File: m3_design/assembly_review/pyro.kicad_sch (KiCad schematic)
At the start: 32 parts, among them J120 ARM: RAW / BUS2 / BUS1 / RAW, J121 E1- / E1+ / E2+ / E2-, Q124 AON7524, Q125 AON7524

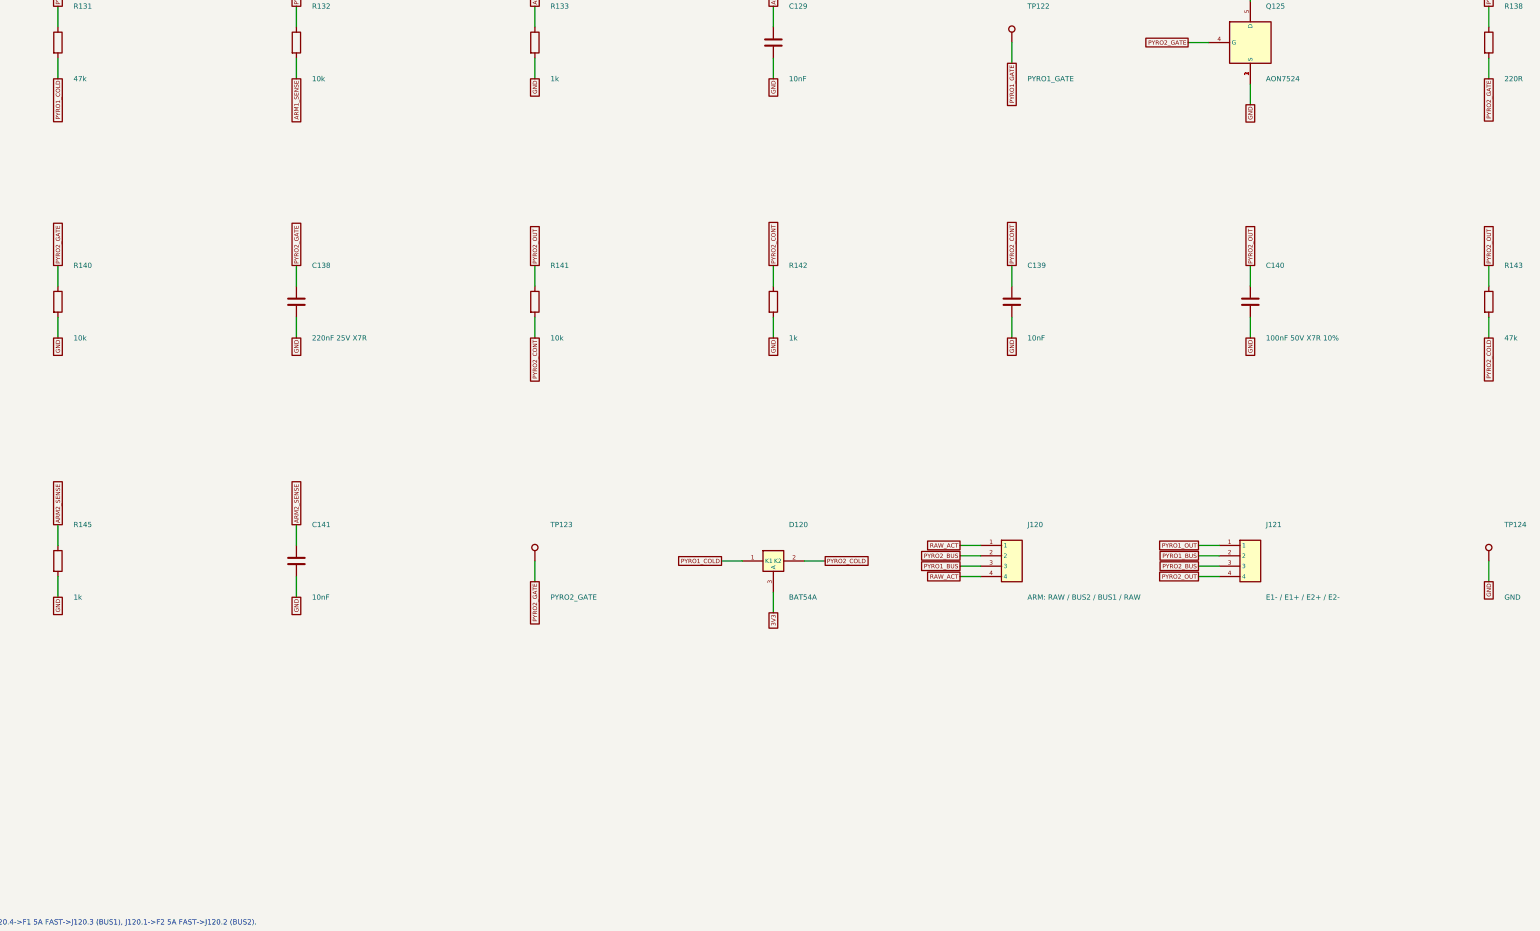
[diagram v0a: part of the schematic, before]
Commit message: Limit a shorted igniter to ~4 A: R134/R135 2 ohm pulse resistors, 10k cold pull-ups
Simulation of R2 as merged showed that firing into a shorted igniter pulled
BAT_IN below 5 V for 4-20 ms until the 5 A arming fuse melted (MCU reset,
channel 2 lost) and overstressed the AON7524 at a fresh pack.

- R134/R135 Bourns CRM2512-FX-2R00ELF (C3013496) in series between each fused
  bus and the igniter terminal (new nets PYRO1_IGN/PYRO2_IGN); arm sense stays
  on the plug side. Placed in line on the bus straps; TP124 moved, four
  references moved to free silkscreen.
- R131/R143 cold pull-ups 47k -> 10k for plug-out self-test margin.
- check_actuators.py contract updated (+ negative cases verified by hand).
- sim_r2 models the fix as drawn: all current-design cases pass; the merged
  design is kept as OLD-FAIL comparison rows.
- Firmware requirements recorded: 20 ms fire pulse, resume after reset.

DRC 0 / unconnected 0 / parity 0 / ERC 0, audit OK; diagnostics 173, firmware
112, quality_audit 12 tests pass.

Co-Authored-By: Claude Opus 5.5 (1M context) <noreply@anthropic.com>
Claude-Session: https://claude.ai/code/session_01DdkfTxR7SVyv9xZNmPk9vB
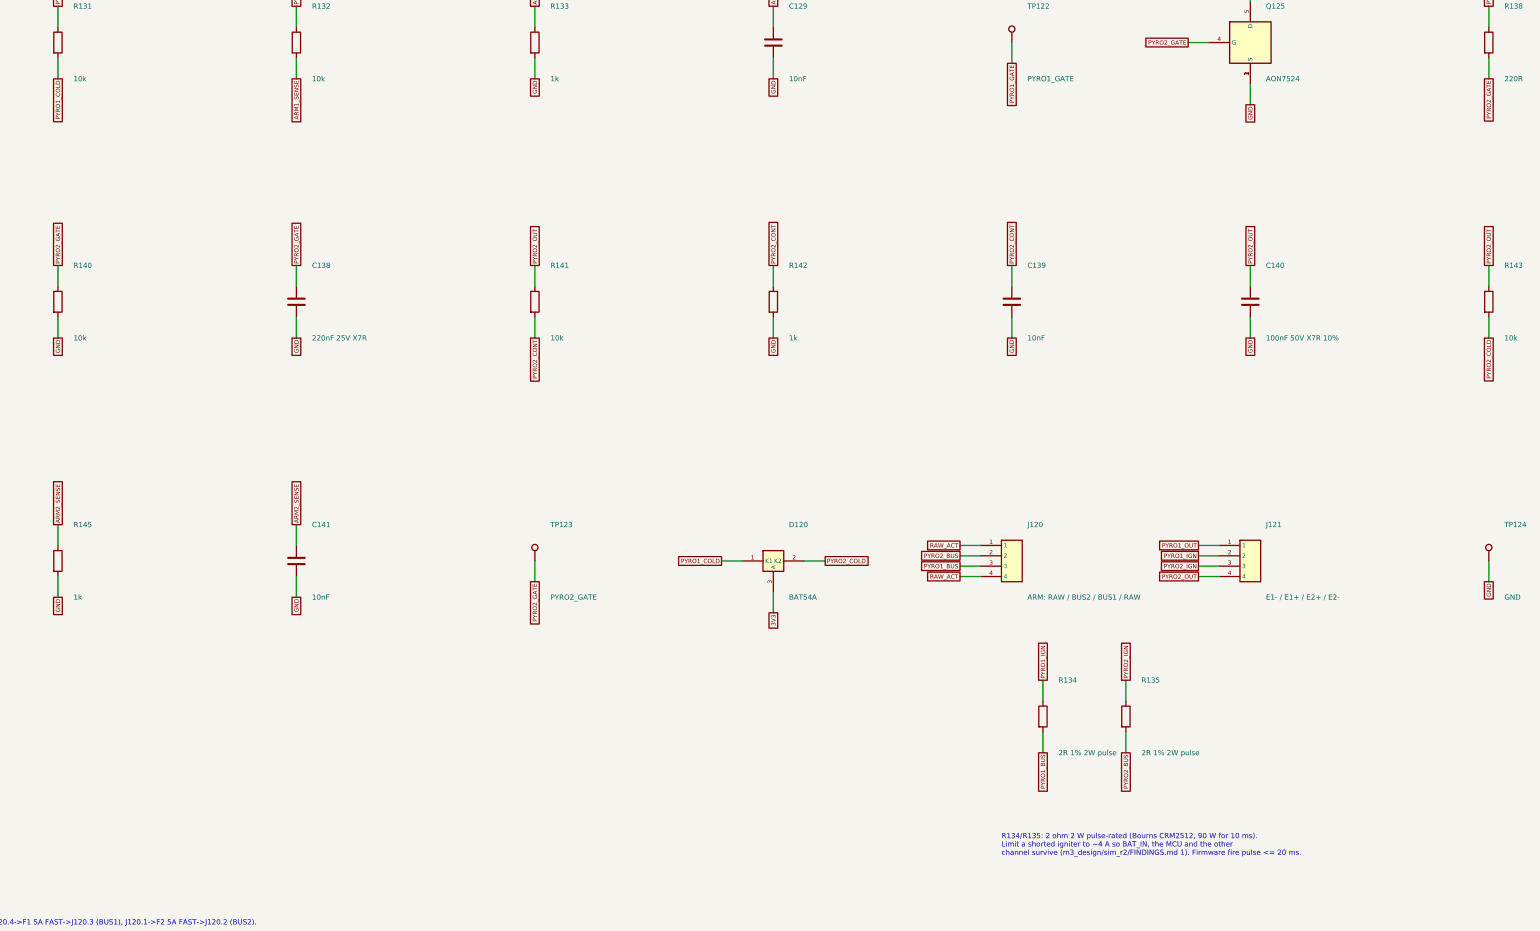
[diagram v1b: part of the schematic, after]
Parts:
- added R134, R135: 2R 1% 2W pulse, rocket:R2512, symbol M3:R
- R131, R143: value 47k -> 10k; LCSC C25792 -> C25744
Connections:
- net PYRO1_BUS: now also R134.2; no longer J121.2
- net PYRO2_BUS: now also R135.2; no longer J121.3
- new net PYRO1_IGN: J121.2, R134.1
- new net PYRO2_IGN: J121.3, R135.1
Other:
- note added: "R134/R135: 2 ohm 2 W pulse-rated (Bourns CRM2512, 90 W for 10 ms). Limit a shorted igniter to ~4 A so BAT_IN, the MCU and the other channel survive (m3_design/sim_r2/FINDINGS.md 1). Firmware fire pulse <= 20 ms."
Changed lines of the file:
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@@
 					(size 1.27 1.27))
 				(justify left)))
-		(property "Value" "47k"
+		(property "Value" "10k"
 			(at 102.87 123.19 0)
 			(effects
@@
 				(font
 					(size 1.27 1.27))))
-		(property "LCSC" "C25792"
+		(property "LCSC" "C25744"
 			(at 99.06 114.3 0)
 			(hide yes)
@@
 					(reference "R132")
 					(unit 1)))))
+	(symbol
+		(lib_id "M3:R")
+		(at 340.36 279.4 0)
+		(unit 1)
+		(in_bom yes)
+		(on_board yes)
+		(dnp no)
+		(property "Reference" "R134"
+			(at 344.17 270.51 0)
+			(effects
+				(font
+					(size 1.27 1.27))
+				(justify left)))
+		(property "Value" "2R 1% 2W pulse"
+			(at 344.17 288.29 0)
+			(effects
+				(font
+					(size 1.27 1.27))
+				(justify left)))
+		(property "Footprint" "rocket:R2512"
+			(at 340.36 279.4 0)
+			(hide yes)
+			(effects
+				(font
+					(size 1.27 1.27))))
+		(property "Datasheet" ""
+			(at 340.36 279.4 0)
+			(hide yes)
+			(effects
+				(font
+					(size 1.27 1.27))))
+		(property "LCSC" "C3013496"
+			(at 340.36 279.4 0)
+			(hide yes)
+			(effects
+				(font
+					(size 1.27 1.27))))
+		(property "Manufacturer" "Bourns"
+			(at 340.36 279.4 0)
+			(hide yes)
+			(effects
+				(font
+					(size 1.27 1.27))))
+		(property "Manufacturer Part" "CRM2512-FX-2R00ELF"
+			(at 340.36 279.4 0)
+			(hide yes)
+			(effects
+				(font
+					(size 1.27 1.27))))
+		(instances
+			(project "m3"
+				(path "/6007a7db-6a58-5660-8beb-956dea045ff8/a44998d3-a410-5959-9243-41a16cadc930"
+					(reference "R134")
+					(unit 1)))))
+	(wire
+		(pts
+			(xy 340.36 275.59)
+			(xy 340.36 270.51))
+		(stroke
+			(width 0)
+			(type default))
+)
+	(global_label "PYRO1_IGN"
+		(shape passive)
+		(at 340.36 270.51 90)
+		(effects
+			(font
+				(size 1.05 1.05))
+			(justify left))
+)
+	(wire
+		(pts
+			(xy 340.36 283.21)
+			(xy 340.36 288.29))
+		(stroke
+			(width 0)
+			(type default))
+)
+	(global_label "PYRO1_BUS"
+		(shape passive)
+		(at 340.36 288.29 270)
+		(effects
+			(font
+				(size 1.05 1.05))
+			(justify right))
+)
+	(symbol
+		(lib_id "M3:R")
+		(at 360.68 279.4 0)
+		(unit 1)
+		(in_bom yes)
+		(on_board yes)
+		(dnp no)
+		(property "Reference" "R135"
+			(at 364.49 270.51 0)
+			(effects
+				(font
+					(size 1.27 1.27))
+				(justify left)))
+		(property "Value" "2R 1% 2W pulse"
+			(at 364.49 288.29 0)
+			(effects
+				(font
+					(size 1.27 1.27))
+				(justify left)))
+		(property "Footprint" "rocket:R2512"
+			(at 360.68 279.4 0)
+			(hide yes)
+			(effects
+				(font
+					(size 1.27 1.27))))
+		(property "Datasheet" ""
+			(at 360.68 279.4 0)
+			(hide yes)
+			(effects
+				(font
+					(size 1.27 1.27))))
+		(property "LCSC" "C3013496"
+			(at 360.68 279.4 0)
+			(hide yes)
+			(effects
+				(font
+					(size 1.27 1.27))))
+		(property "Manufacturer" "Bourns"
+			(at 360.68 279.4 0)
+			(hide yes)
+			(effects
+				(font
+					(size 1.27 1.27))))
+		(property "Manufacturer Part" "CRM2512-FX-2R00ELF"
+			(at 360.68 279.4 0)
+			(hide yes)
+			(effects
+				(font
+					(size 1.27 1.27))))
+		(instances
+			(project "m3"
+				(path "/6007a7db-6a58-5660-8beb-956dea045ff8/a44998d3-a410-5959-9243-41a16cadc930"
+					(reference "R135")
+					(unit 1)))))
+	(wire
+		(pts
+			(xy 360.68 275.59)
+			(xy 360.68 270.51))
+		(stroke
+			(width 0)
+			(type default))
+)
+	(global_label "PYRO2_IGN"
+		(shape passive)
+		(at 360.68 270.51 90)
+		(effects
+			(font
+				(size 1.05 1.05))
+			(justify left))
+)
+	(wire
+		(pts
+			(xy 360.68 283.21)
+			(xy 360.68 288.29))
+		(stroke
+			(width 0)
+			(type default))
+)
+	(global_label "PYRO2_BUS"
+		(shape passive)
+		(at 360.68 288.29 270)
+		(effects
+			(font
+				(size 1.05 1.05))
+			(justify right))
+)
+	(text "R134/R135: 2 ohm 2 W pulse-rated (Bourns CRM2512, 90 W for 10 ms).\nLimit a shorted igniter to ~4 A so BAT_IN, the MCU and the other\nchannel survive (m3_design/sim_r2/FINDINGS.md 1). Firmware fire pulse <= 20 ms."
+		(exclude_from_sim no)
+		(at 330.2 313.69 0)
+		(effects
+			(font
+				(size 1.27 1.27))
+			(justify left bottom))
+)
 	(wire
 		(pts
@@
 					(size 1.27 1.27))
 				(justify left)))
-		(property "Value" "47k"
+		(property "Value" "10k"
 			(at 453.39 186.69 0)
 			(effects
@@
 				(font
 					(size 1.27 1.27))))
-		(property "LCSC" "C25792"
+		(property "LCSC" "C25744"
 			(at 449.58 177.8 0)
 			(hide yes)
@@
 			(type default))
 )
-	(global_label "PYRO1_BUS"
+	(global_label "PYRO1_IGN"
 		(shape passive)
 		(at 378.46 240.03 180)
@@
 			(type default))
 )
-	(global_label "PYRO2_BUS"
+	(global_label "PYRO2_IGN"
 		(shape passive)
 		(at 378.46 242.57 180)

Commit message: M3-ASSY-R4: R3 validation fixes, new IMU, fault-tolerant pyro sensing
The board, schematic sheets and footprint library are generated from
R3 (533af8e) by m3_design/r4_build.sh (r4_lib.py, r4_sch.py,
r4_pcb.py). docs/REQUIREMENTS.md states what the board must do;
docs/M3_R4.md records every change, the thirteen evaluation passes
(twelve independent reviews) and the accepted deviations.

- IMU: ST LSM6DSV320X (16 g and 320 g, 4000 dps)
- Pyro: black ARM and orange igniter terminals, eight pyro spacing
  rules in m3.kicad_dru, sense dividers of 2 x 5.1k over 2 x 2k in
  parallel, 4.7k at each ADC pin (R168-R172)
- Pull-pin on a JST PH connector; JLC tooling holes
- Fab: Standard PCBA, 84 BOM lines, 205 placed parts, $80.12 per board
  at five boards (tools/jlc_cost.py); placement rotations verified
- Gate: tools/check.sh DRC 0, unconnected 0, schematic parity 0, ERC 0,
  audit OK; m3_design/check_actuators.py OK

Nothing has been built or measured, and there is no R4 firmware. The
open owner decisions and the bench tests are listed in STATUS.md.

Co-Authored-By: Claude Opus 5.5 <noreply@anthropic.com>
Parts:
- removed TP124: GND, rocket:M3_TestPad_1.5, symbol M3:TestPoint
- added J124: ARM CH1: BUS1 / RAW, rocket:M3_DB128L_2P_BK, symbol M3:Conn_1x2
- added J125: IGNITER 2: E2+ / E2-, rocket:M3_DB128L_2P, symbol M3:Conn_1x2
- added R173, R174, R175, R176: 5.1k, rocket:R0402, symbol M3:R
- added R178, R179, R180, R181: 2k, rocket:R0402, symbol M3:R
- C128, C140: LCSC C1591 -> C161115; Manufacturer Samsung Electro-Mechanics -> Murata; Manufacturer Part CL10B104KB8NNNC -> GCJ188R71H104KA12D
- J120: value ARM: RAW / BUS2 / BUS1 / RAW -> ARM CH2: RAW / BUS2; footprint rocket:M3_DB128V_4P -> rocket:M3_DB128L_2P_BK; symbol M3:Conn_1x4 -> M3:Conn_1x2; LCSC C2915641 -> C430601; LCSC Part (none) -> C430601; Manufacturer (none) -> DORABO; Manufacturer Part (none) -> DB128L-5.08-2P-BK-S
- J121: value E1- / E1+ / E2+ / E2- -> IGNITER 1: E1- / E1+; footprint rocket:M3_DB128V_4P -> rocket:M3_DB128L_2P; symbol M3:Conn_1x4 -> M3:Conn_1x2; LCSC C2915641 -> C430603; LCSC Part (none) -> C430603; Manufacturer (none) -> DORABO; Manufacturer Part (none) -> DB128L-5.08-2P-OG-S
- R129, R132, R141, R144: value 10k -> 5.1k; LCSC C25744 -> C25905
- R130, R133, R142, R145: value 1k -> 2k; LCSC C11702 -> C4109
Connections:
- net ARM1_SENSE: now also R175.2, R180.1; no longer R132.2
- net ARM2_SENSE: now also R176.2, R181.1; no longer R144.2
- net GND: now also R178.2, R179.2, R180.2, R181.2
- net PYRO1_BUS: now also J124.1; no longer J120.3
- net PYRO1_CONT: now also R178.1
- net PYRO1_OUT: now also R173.1; no longer R129.1
- net PYRO2_CONT: now also R179.1
- net PYRO2_IGN: now also J125.1; no longer J121.3
- net PYRO2_OUT: now also J125.2, R174.1; no longer J121.4, R141.1
- net RAW_ACT: now also J124.2; no longer J120.4
- new net ARM1_SENSE_MID: R132.2, R175.1
- new net ARM2_SENSE_MID: R144.2, R176.1
- new net PYRO1_CONT_MID: R129.1, R173.2
- new net PYRO2_CONT_MID: R141.1, R174.2
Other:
- note added: "CONT = (2 x 5.1k)/(2 x 2k parallel) from each drain (open detector only, CIRCUIT_REVIEW 2.9). ARMn_SENSE = the same from each fused bus."
- note added: "D120 + R131/R143 (10k): cold pull-up of both drains (FMEA H-1) for plug-out FET-short detection. In flight: log only, never veto (F-10)."
- note added: "Igniter 1 across J121.1-2, igniter 2 across J125.1-2. Each pin order is reversal-symmetric within its channel."
- note added: "Pass 11: each divider top is 2 x 5.1k in series (R173 + R129, R174 + R141 from the drains; R132 + R175, R144 + R176 from the buses); pass 12: each bottom is 2 x 2k in parallel (R130 + R178, R142 + R179, R133 + R180, R145 + R181). Ratio 1/11.2. One shorted or open 0402 leaves its ADC node <= 1.4 V (<= 3.3 V at the 19.9 V clamp) and the igniter <= 1.4 mA; R168-R171 (4.7k at the MCU pins) stay as th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"
- note added: "Two independent channels (FMEA H-5). ARM links: J124.2 (RAW) -> F1 5A FAST -> J124.1 (BUS1); J120.1 (RAW) -> F2 5A FAST -> J120.2 (BUS2). R4: DB128L 2P pairs, ARM terminals black, igniter terminals orange."
- note removed: "CONT = 10k/1k from drain (open detector only, CIRCUIT_REVIEW 2.9). ARMn_SENSE = 10k/1k from each fused bus."
- note removed: "D120 + 47k: cold pull-up of both drains (FMEA H-1) for plug-out FET-short detection. In flight: log only, never veto (F-10)."
- note removed: "Igniter 1 across J121.1-2, igniter 2 across J121.3-4. Both terminal pin orders are reversal-symmetric."
- note removed: "Two independent channels (FMEA H-5). ARM plug = 4-wire, 2-fuse link: J120.4->F1 5A FAST->J120.3 (BUS1), J120.1->F2 5A FAST->J120.2 (BUS2)."
